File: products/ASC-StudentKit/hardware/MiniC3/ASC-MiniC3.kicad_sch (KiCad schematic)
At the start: 36 parts, among them J1 PUMP, J3 AUX, J4 FLOW, J5 I2C, J6 RELAY 230V, K1 HF46F/005-HS1, Q1 AO3400A, Q2 AO3400A, U1 ESP32-C3 Super Mini, U2 DS1307Z+, Y1 32.768k 12.5pF

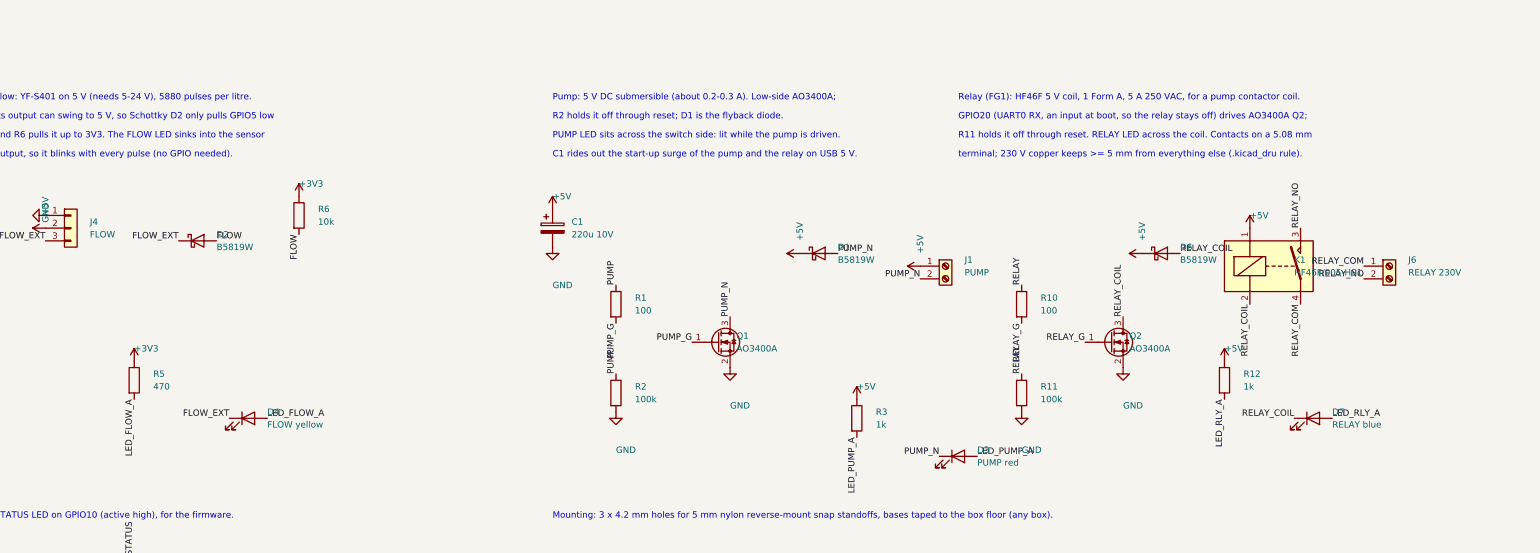
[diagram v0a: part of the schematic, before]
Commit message: ASC Mini-C3: ULN2003A driver, combo flow connector, assembly markings
- ULN2003A (LCSC C7512) drives the pump (ch 1+2) and the relay (ch 3);
  replaces 2 x AO3400A, 3 x B5819W and 4 resistors, as on FG1
- Flow input: one footprint takes a JST-XH (bench) or a 3.5 mm 3-pole
  screw terminal (FG1 field cable)
- Screw terminals now Phoenix PT-1,5 3.5 mm (KF350 type, library 3D);
  relay output is a pluggable MSTBVA 5.08 header like FG1's
- 1206 LEDs for hand soldering; ref + value labels on every part
  (R3 1K, U3 ULN2003 ...), "1" at IC pin 1, "+" at LED/diode anodes;
  back reads "Agri Sensors and Controls  Oct 2026"
- Re-routed, DRC clean (mains 5 mm), panel and fab regenerated
- Sourcing BOM: 1206 LED and ULN2003A LCSC numbers, CR2032 holder as an
  alternative to the tabbed cell; kit about Rs 967

Co-Authored-By: Claude Opus 5.5 <noreply@anthropic.com>
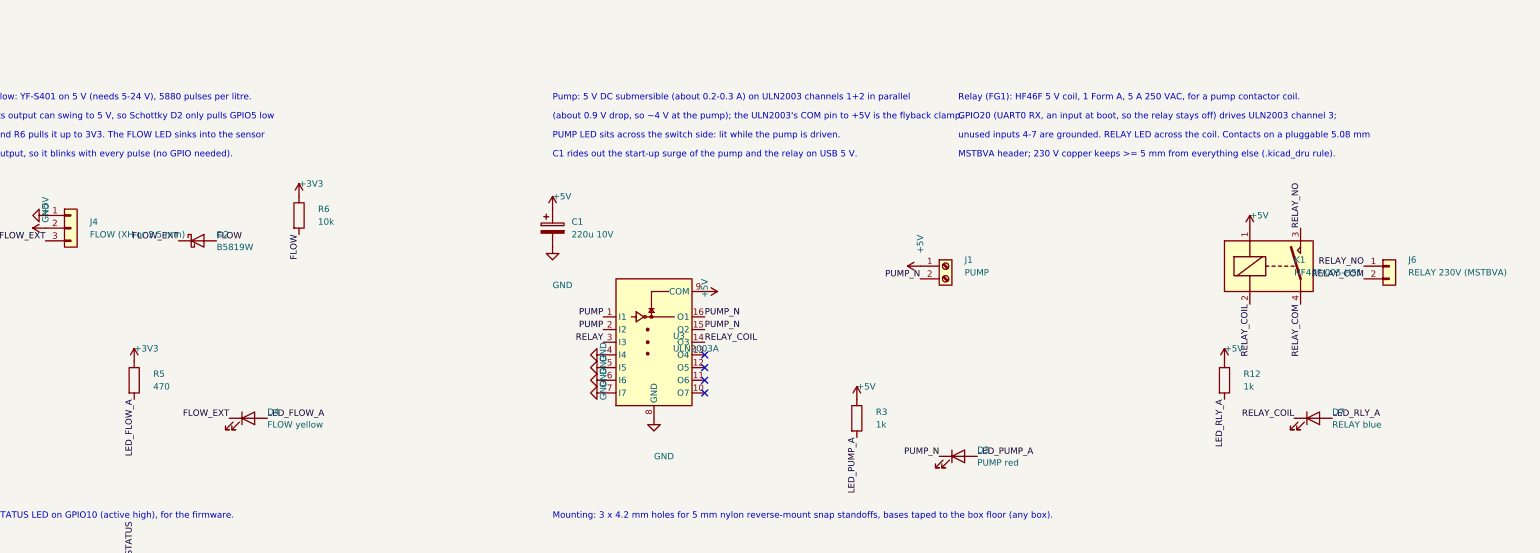
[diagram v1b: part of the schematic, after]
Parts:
- removed D1, D6: B5819W, Diode_SMD:D_SOD-123, symbol Device:D_Schottky
- removed J6: RELAY 230V, TerminalBlock_MetzConnect:TerminalBlock_MetzConnect_Type101_RT01602HBWC_1x02_P5.08mm_Horizontal, symbol Connector:Screw_Terminal_01x02
- removed Q1, Q2: AO3400A, Package_TO_SOT_SMD:SOT-23, symbol Transistor_FET:AO3400A
- removed R1, R10: 100, Resistor_SMD:R_0805_2012Metric, symbol Device:R
- removed R11, R2: 100k, Resistor_SMD:R_0805_2012Metric, symbol Device:R
- added J6: RELAY 230V (MSTBVA), Connector_Phoenix_MSTB:PhoenixContact_MSTBVA_2,5_2-G-5,08_1x02_P5.08mm_Vertical, symbol Connector_Generic:Conn_01x02
- added U3: ULN2003A, Package_SO:SOIC-16_3.9x9.9mm_P1.27mm, symbol Transistor_Array:ULN2003A
- D3, D4, D5, D7: footprint LED_SMD:LED_0805_2012Metric -> LED_SMD:LED_1206_3216Metric
- J1: footprint TerminalBlock_MetzConnect:TerminalBlock_MetzConnect_Type086_RT03402HBLC_1x02_P3.81mm_Horizontal -> TerminalBlock_Phoenix:TerminalBlock_Phoenix_PT-1,5-2-3.5-H_1x02_P3.50mm_Horizontal
- J3: footprint TerminalBlock_MetzConnect:TerminalBlock_MetzConnect_Type086_RT03405HBLC_1x05_P3.81mm_Horizontal -> TerminalBlock_Phoenix:TerminalBlock_Phoenix_PT-1,5-5-3.5-H_1x05_P3.50mm_Horizontal
- J4: value FLOW -> FLOW (XH or 3.5 mm); footprint Connector_JST:JST_XH_B3B-XH-A_1x03_P2.50mm_Vertical -> ASC:Flow_XH3_or_PT-1,5-3-3.5mm
- J5: footprint TerminalBlock_MetzConnect:TerminalBlock_MetzConnect_Type086_RT03404HBLC_1x04_P3.81mm_Horizontal -> TerminalBlock_Phoenix:TerminalBlock_Phoenix_PT-1,5-4-3.5-H_1x04_P3.50mm_Horizontal
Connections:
- net +5V: now also U3.9 (COM)
- net GND: now also U3.4 (I4), U3.5 (I5), U3.6 (I6), U3.7 (I7), U3.8 (GND)
- net PUMP: now also U3.1 (I1), U3.2 (I2)
- net PUMP_N: now also U3.15 (O2), U3.16 (O1)
- net RELAY: now also U3.3 (I3)
- net RELAY_COIL: now also U3.14 (O3)
- net RELAY_COM: now also J6.2 (Pin_2)
- net RELAY_NO: now also J6.1 (Pin_1)
- no-connect marks 5 -> 9
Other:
- note added: "(about 0.9 V drop, so ~4 V at the pump); the ULN2003's COM pin to +5V is the flyback clamp."
- note added: "GPIO20 (UART0 RX, an input at boot, so the relay stays off) drives ULN2003 channel 3;"
- note added: "MSTBVA header; 230 V copper keeps >= 5 mm from everything else (.kicad_dru rule)."
- note added: "Pump: 5 V DC submersible (about 0.2-0.3 A) on ULN2003 channels 1+2 in parallel"
- note added: "unused inputs 4-7 are grounded. RELAY LED across the coil. Contacts on a pluggable 5.08 mm"
- note removed: "GPIO20 (UART0 RX, an input at boot, so the relay stays off) drives AO3400A Q2;"
- note removed: "Pump: 5 V DC submersible (about 0.2-0.3 A). Low-side AO3400A;"
- note removed: "R11 holds it off through reset. RELAY LED across the coil. Contacts on a 5.08 mm"
- note removed: "R2 holds it off through reset; D1 is the flyback diode."
- note removed: "terminal; 230 V copper keeps >= 5 mm from everything else (.kicad_dru rule)."

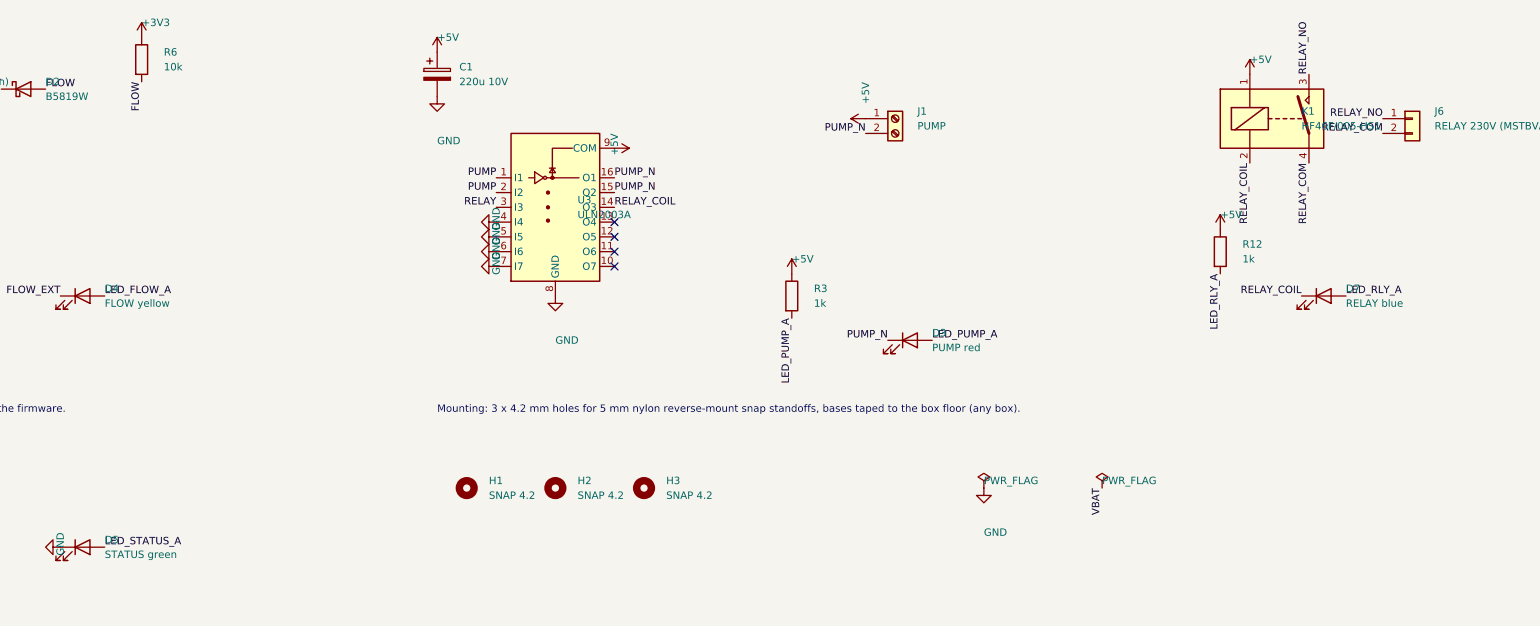
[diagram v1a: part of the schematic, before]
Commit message: ASC Mini-C3: LED colours, relay header turned, date line
- LEDs: PUMP and RLY yellow (C30584802), STATUS red (C37635751),
  FLOW yellow-green (C28310441, ~2 V: it runs from 3.3 V into the
  sensor output); the Super Mini's blue LED on GPIO8 is the WiFi LED
- Relay MSTBVA header turned 180 so the curved side faces inward, as on
  FG1; pins re-mapped (1 COM, 2 NO), mains tracks re-drawn, 5.00 mm
- Back silkscreen: "Oct 2026" on its own line
- Re-routed, DRC clean; panel, fab, BOM/CPL and sourcing regenerated

Co-Authored-By: Claude Opus 5.5 <noreply@anthropic.com>
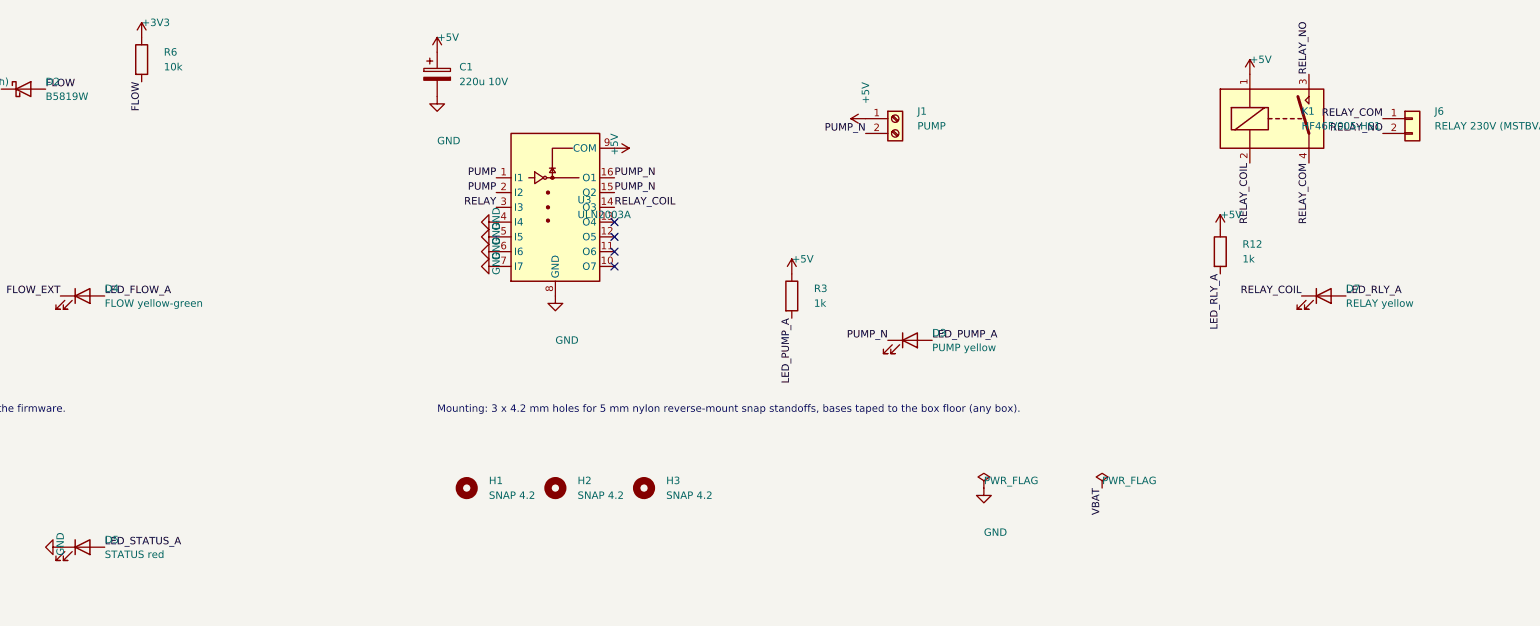
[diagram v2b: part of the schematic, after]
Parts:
- D3: value PUMP red -> PUMP yellow
- D4: value FLOW yellow -> FLOW yellow-green
- D5: value STATUS green -> STATUS red
- D7: value RELAY blue -> RELAY yellow
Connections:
- net RELAY_COM: now also J6.1 (Pin_1); no longer J6.2 (Pin_2)
- net RELAY_NO: now also J6.2 (Pin_2); no longer J6.1 (Pin_1)

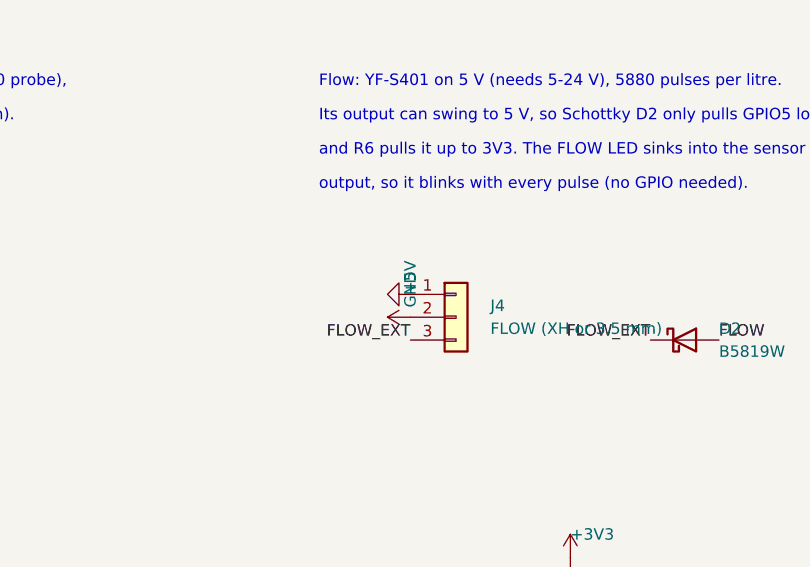
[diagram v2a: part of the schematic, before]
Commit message: ASC Mini-C3: slot-and-tab panel, flow pinout fix, BOM rates
- Panel now 98 x 98: 4 Minis + 2 AHT20 sticks, 2 mm routed slots with
  tabs and 0.5 mm mouse-bite holes (78, NPTH); no V-cut, as WhyPCB asked
  (JLC charges extra for V-cut). Zip carries a drawing and PANEL-README.
- Flow connector pinout fixed to the YF-S401 wiring: 1 = 5V (red),
  2 = GND (black, middle), 3 = SIG (yellow); silkscreen "FLOW S G 5V".
  Re-routed, DRC clean, mains clearance 5.00 mm.
- BOM: WhyPCB Rs 1,500 / 5 panels, Rs 2,000 / 10 panels (Rs 50 per Mini);
  kit about Rs 979; 2-kit sample about Rs 4,840 + LCSC shipping

Co-Authored-By: Claude Opus 5.5 <noreply@anthropic.com>
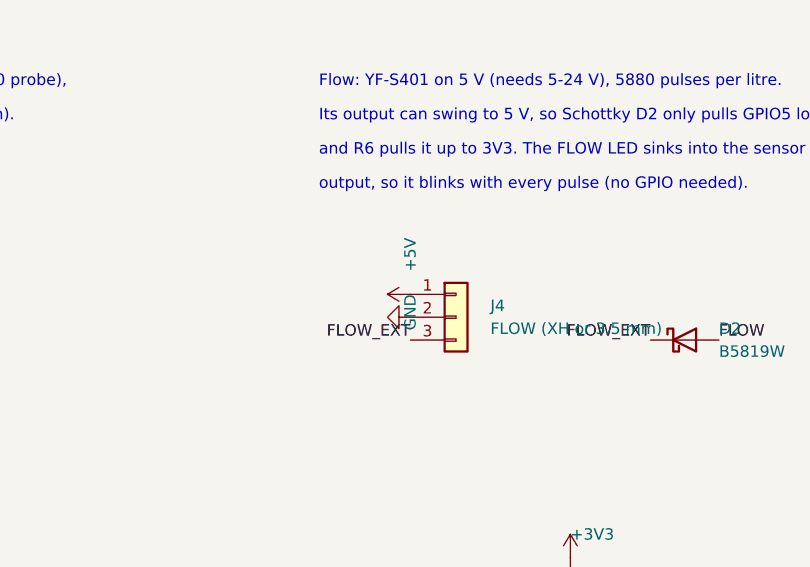
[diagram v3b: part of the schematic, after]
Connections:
- net +5V: now also J4.1 (Pin_1); no longer J4.2 (Pin_2)
- net GND: now also J4.2 (Pin_2); no longer J4.1 (Pin_1)
